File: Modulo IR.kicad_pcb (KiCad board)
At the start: 2 copper layers, 17.3 x 29.2 mm, 14 parts, among them U1 LM358N, U10 100nF, U12 TCRT5000, U13 100R, U3 1K, U5 20K, U6 10K, U7 10k, U8 CON3_ET, U9 LED

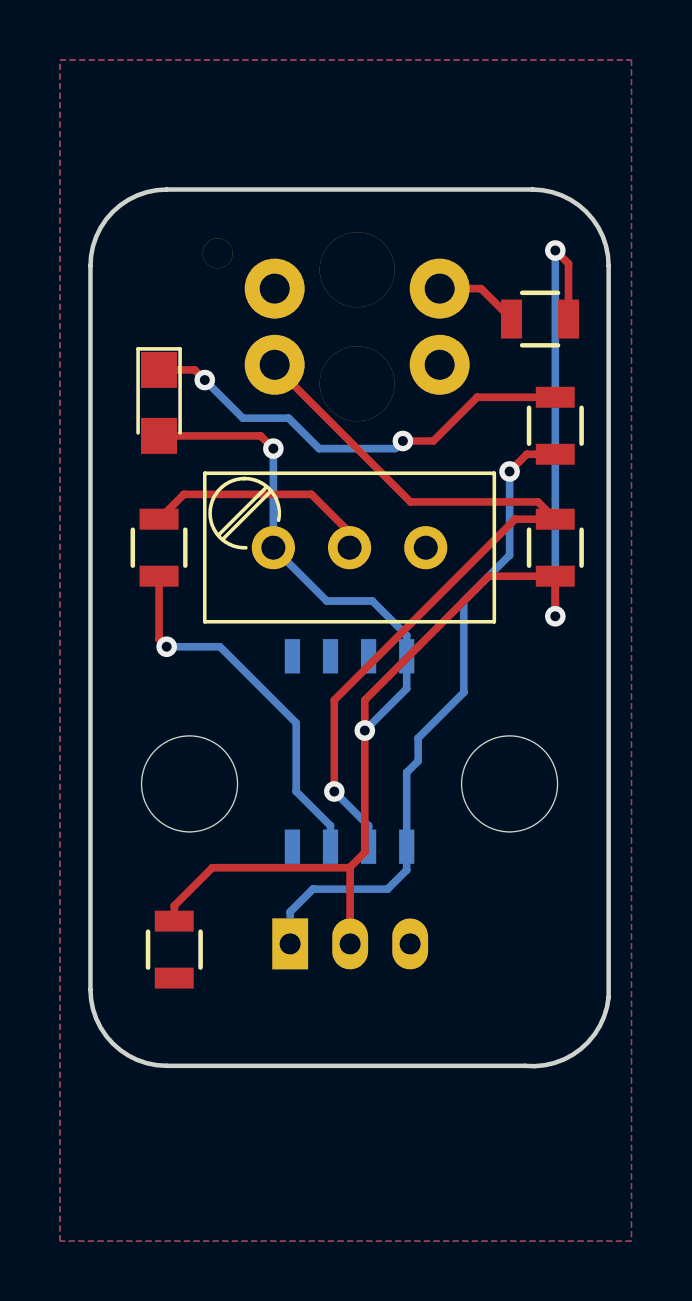
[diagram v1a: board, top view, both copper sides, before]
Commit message: Arreglado el error con el footprint del TCRT5000
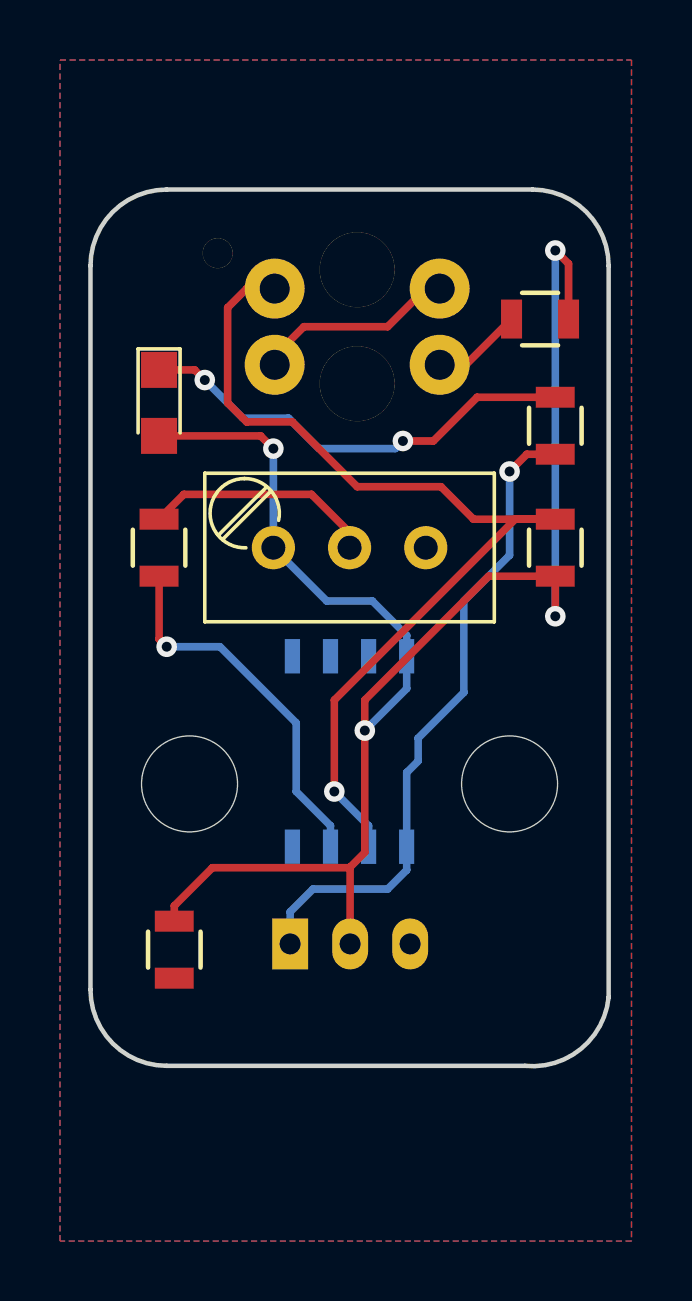
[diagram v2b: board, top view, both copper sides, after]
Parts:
- U1: footprint SMD_Packages:SOIC-8-N -> lib_fp:SOIC-8-N
- U10, U13, U3, U5, U6: footprint Resistors_SMD:R_0805 -> lib_fp:R_0805
- U12: footprint cyclophone:TCRT5000 -> lib_fp:TCRT5000
- U7: footprint Potentiometers:Potentiometer_Trimmer_Bourns_3296W -> lib_fp:Potentiometer_Trimmer_Bourns_3296W
- U8: footprint Connectors_JST:JST_PH_S3B-PH-K_03x2.00mm_Angled -> lib_fp:JST_PH_S3B-PH-K_03x2.00mm_Angled
- U9: footprint LEDs:LED_0805 -> lib_fp:LED_0805
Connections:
- U12 pad 1: GNDREF -> Net-(U12-Pad1)
- U12 pad 2: Net-(U12-Pad2) -> GNDREF
- U12 pad 3: A0 -> GNDREF
- U12 pad 4: GNDREF -> A0
- U13 pad 2: Net-(U12-Pad2) -> Net-(U12-Pad1)
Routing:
- net GNDREF: track 0.18 -> 6.95 mm
- net A0: track 26.9 -> 32.9 mm
- net Net-(U12-Pad1): track 0.00 -> 3.03 mm
- net Net-(U12-Pad2): track 2.82 -> 0.00 mm
